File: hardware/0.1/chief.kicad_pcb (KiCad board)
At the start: 2 copper layers, 84.3 x 65 mm, 54 parts, among them J1 USB_C_Receptacle_USB2.0, Q1 DTC123J, Q2 BSS138, SW1 Encoder_MX_RGB, SW10 Encoder_MX_RGB, SW11 MX_RGB, SW12 MX_RGB, SW13 SW_Push, SW2 MX_RGB, SW3 MX_RGB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

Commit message: sorry Bing
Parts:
- removed RN5: 5K1, Resistor_SMD:R_Array_Convex_4x0603
- added R6: 5K1, Resistor_SMD:R_0603_1608Metric, B.Cu at (147.1, 74.8)
- added R7: 5K1, Resistor_SMD:R_0603_1608Metric, B.Cu at (145.6, 74.8)
- moved C13 32.2 mm to (174.1, 82.1), turned to 90 degrees
- moved C6 30.3 mm to (111.6, 82.1), turned to 90 degrees
- moved C5 29.9 mm to (160.6, 73.3), turned to 0 degrees
- moved C10 25.3 mm to (116.9, 82.1), turned to 90 degrees
- moved C9 24.7 mm to (168.8, 82.1), turned to 90 degrees
- moved C1 20.2 mm to (140.2, 77.0), turned to 0 degrees
- moved U1 17.5 mm to (140.4, 79.8), turned to 270 degrees
- moved C12 16.2 mm to (155.0, 82.1), turned to 90 degrees
- moved C14 15.0 mm to (135.1, 97.9), turned to 180 degrees
- moved C7 14.9 mm to (130.7, 82.1), turned to 90 degrees
- moved C2 14.7 mm to (140.3, 82.5), turned to 0 degrees
- moved C11 11.4 mm to (135.9, 82.1)
- moved C8 11.4 mm to (149.7, 82.1)
- moved C3 7.93 mm to (139.8, 68.5)
- moved R2 6.03 mm to (160.6, 71.7)
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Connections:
- J1 pad A8: Net-(J1-PadA8) -> (no net)
- J1 pad B8: Net-(J1-PadB8) -> (no net)
- SW12 pad 4: Net-(SW12-Pad4) -> (no net)
- U1 pad 4: Net-(U1-Pad4) -> (no net)
- U3 pad 10: /SW12 -> (no net)
- U3 pad 11: Net-(U3-Pad11) -> (no net)
- U3 pad 12: Net-(U3-Pad12) -> (no net)
- U3 pad 13: Net-(U3-Pad13) -> (no net)
- U3 pad 2: /SW9 -> (no net)
- U3 pad 21: Net-(U3-Pad21) -> (no net)
- U3 pad 22: Net-(U3-Pad22) -> (no net)
- U3 pad 26: /SW5 -> /ENC2B_DB
- U3 pad 27: /ENC2B_DB -> /SW5
- U3 pad 3: /SW11 -> (no net)
- U3 pad 30: Net-(U3-Pad30) -> (no net)
- U3 pad 31: Net-(U3-Pad31) -> (no net)
- U3 pad 4: Net-(U3-Pad4) -> (no net)
- U3 pad 41: Net-(U3-Pad41) -> /ENC4A_DB
- U3 pad 42: /ENC4A_DB -> /ENC4B_DB
- U3 pad 43: Net-(U3-Pad43) -> /SW11
- U3 pad 45: Net-(U3-Pad45) -> /SW12
- U3 pad 46: /ENC4B_DB -> /SW9
- U3 pad 5: Net-(U3-Pad5) -> (no net)
- U3 pad 6: Net-(U3-Pad6) -> (no net)
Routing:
- net +5V: track 324.2 -> 171.7 mm, vias 12 -> 11
- net /LED1: track 102.6 -> 0.00 mm, vias 2 -> 0
- net GND: track 147.0 -> 46.0 mm, vias 16 -> 42
- net /LED2: track 86.2 -> 0.00 mm
- net Net-(SW4-Pad2): track 48.8 -> 0.00 mm, vias 2 -> 0
- net Net-(SW10-Pad1): track 40.8 -> 0.00 mm, vias 2 -> 0
- net Net-(SW1-Pad2): track 39.9 -> 0.00 mm, vias 4 -> 0
- net Net-(SW11-Pad3): track 39.8 -> 0.00 mm, vias 2 -> 0
- net Net-(SW5-Pad4): track 35.2 -> 0.00 mm, vias 2 -> 0
- net /SW12: track 45.8 -> 28.3 mm
- net Net-(SW6-Pad4): track 45.9 -> 28.5 mm, vias 2 -> 0
- net /SW11: track 49.6 -> 36.4 mm
- net /BOOT0: track 35.3 -> 48.4 mm
- net Net-(SW2-Pad4): track 40.1 -> 29.0 mm, vias 3 -> 2
- net Net-(J1-PadB5): track 19.2 -> 8.62 mm
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
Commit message: moar layout
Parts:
- added D3: WS2812B, LED_SMD:LED_WS2812B_PLCC4_5.0x5.0mm_P3.2mm, B.Cu at (161.9, 104.5)
- added D4: WS2812B, LED_SMD:LED_WS2812B_PLCC4_5.0x5.0mm_P3.2mm, B.Cu at (124.8, 82.0)
- added D5: WS2812B, LED_SMD:LED_WS2812B_PLCC4_5.0x5.0mm_P3.2mm, B.Cu at (123.8, 104.5)
- added D6: WS2812B, LED_SMD:LED_WS2812B_PLCC4_5.0x5.0mm_P3.2mm, B.Cu at (160.1, 82.0)
- added H5: dan, graphics:danandrews, F.Cu at (142.6, 90.7)
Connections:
- SW12 pad 4: (no net) -> /BKLT
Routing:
- net +5V: track 171.7 -> 281.0 mm, vias 11 -> 20
- net /LED2: track 0.00 -> 88.0 mm, vias 0 -> 2
- net /LED1: track 0.00 -> 71.7 mm, vias 0 -> 4
- net Net-(SW5-Pad4): track 0.00 -> 48.5 mm, vias 0 -> 7
- net Net-(SW4-Pad2): track 0.00 -> 45.3 mm, vias 0 -> 2
- net Net-(SW1-Pad2): track 0.00 -> 44.5 mm, vias 0 -> 4
- net Net-(SW10-Pad1): track 0.00 -> 44.2 mm, vias 0 -> 4
- net Net-(SW11-Pad3): track 0.00 -> 29.0 mm, vias 0 -> 2
- net GND: track 46.0 -> 51.8 mm, vias 42 -> 46
- net /SW1: track 49.4 -> 50.9 mm
- net /LED: track 36.8 -> 35.5 mm
- net +3V3: track 183.2 -> 184.3 mm
- net /ENC3B_DB: track 24.7 -> 25.7 mm
- net /ENC3A_DB: track 20.6 -> 21.6 mm
- net /SW2: track 30.6 -> 30.0 mm
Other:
- board text added: "CHIEF"
- board text added: "LED"
- board text added: "PWR"
- board text added: "RST"
- board text added: "bing"

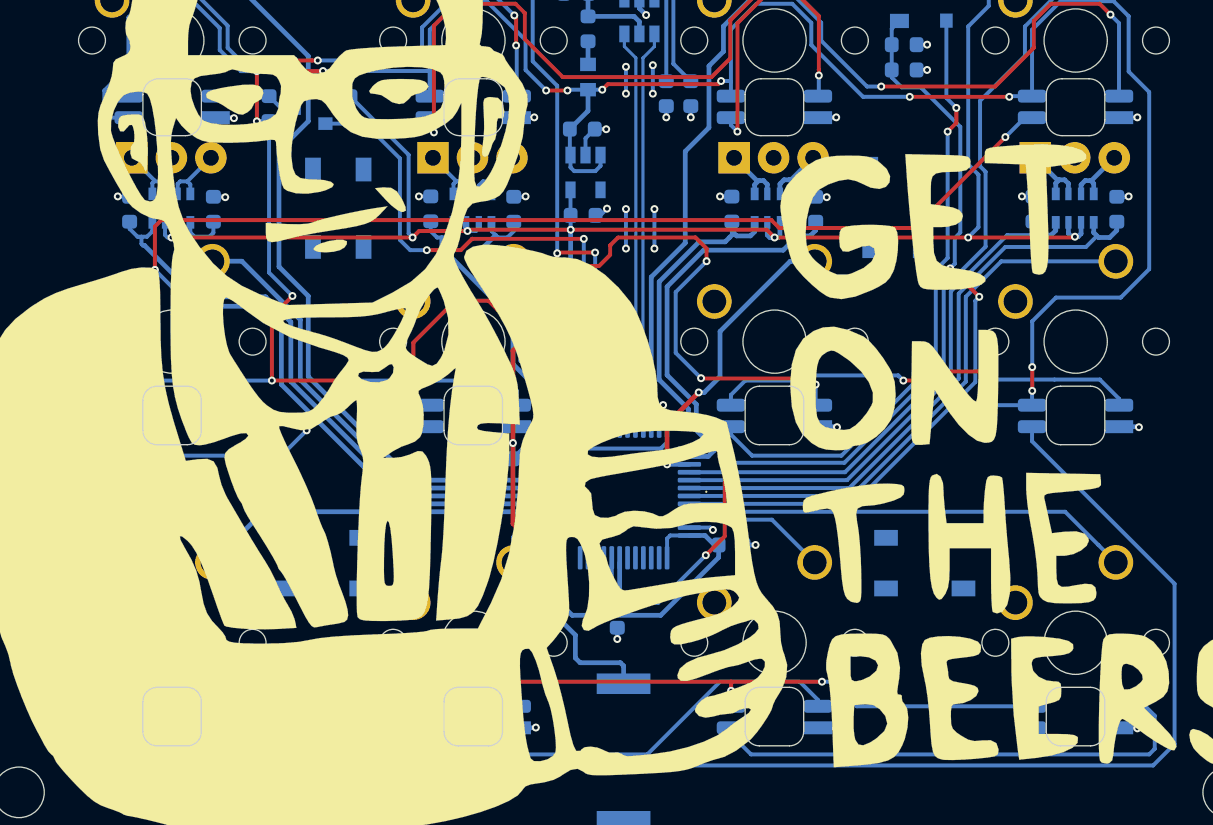
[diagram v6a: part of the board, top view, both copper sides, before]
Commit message: LEDs connected, adjustments to LED/text/image position
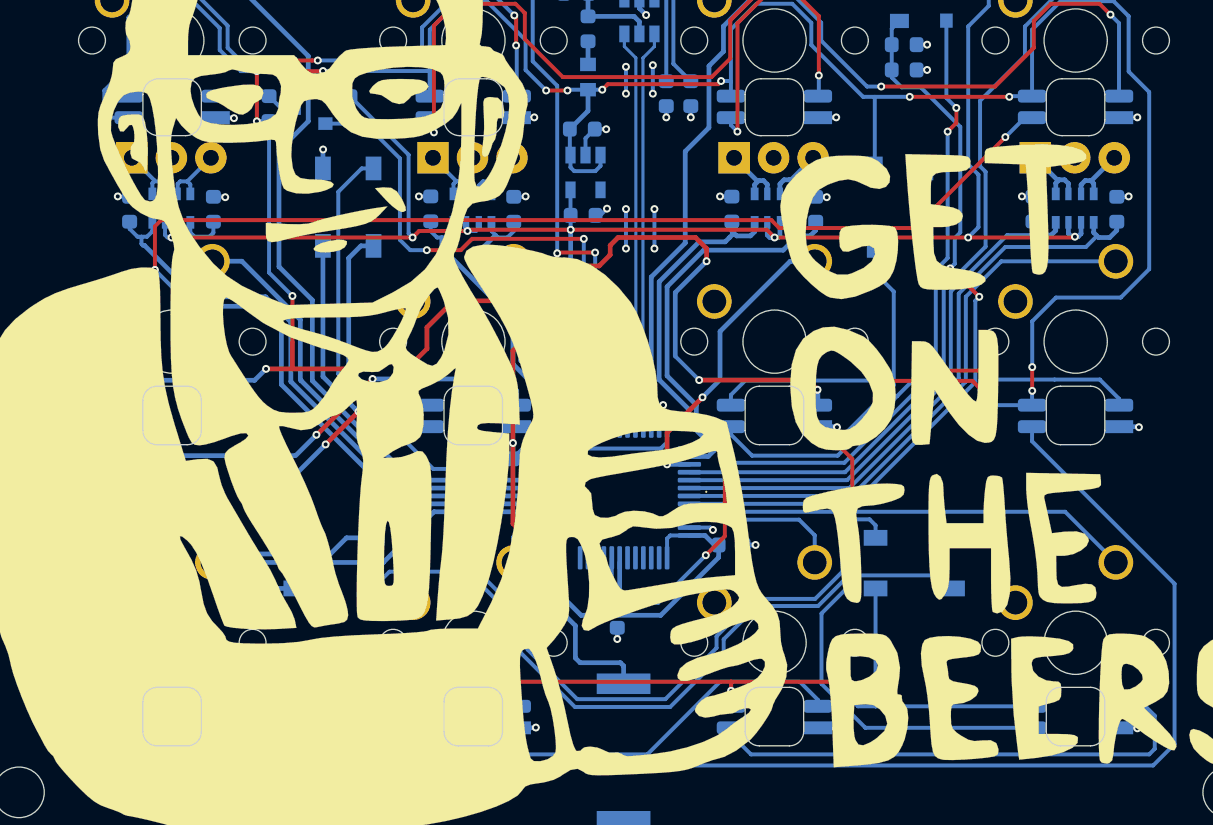
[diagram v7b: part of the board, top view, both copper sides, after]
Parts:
- moved D5 0.73 mm to (124.5, 104.5)
- moved D3 0.66 mm to (161.2, 104.5)
- moved D4 0.63 mm to (125.4, 82.0)
- moved D6 0.29 mm to (160.3, 82.0)
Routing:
- net Net-(D3-Pad2): track 0.00 -> 68.8 mm, vias 0 -> 2
- net Net-(D5-Pad2): track 0.00 -> 62.5 mm, vias 0 -> 2
- net +5V: track 281.0 -> 316.4 mm
- net /BKLT: track 0.00 -> 28.6 mm
- net Net-(D4-Pad2): track 0.00 -> 21.1 mm, vias 0 -> 2
- net GND: track 51.8 -> 56.8 mm, vias 46 -> 50
- net /SW9: track 9.05 -> 10.1 mm
- net Net-(SW5-Pad4): track 48.5 -> 48.6 mm, vias 7 -> 6
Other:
- board text added: "opsbinxu"

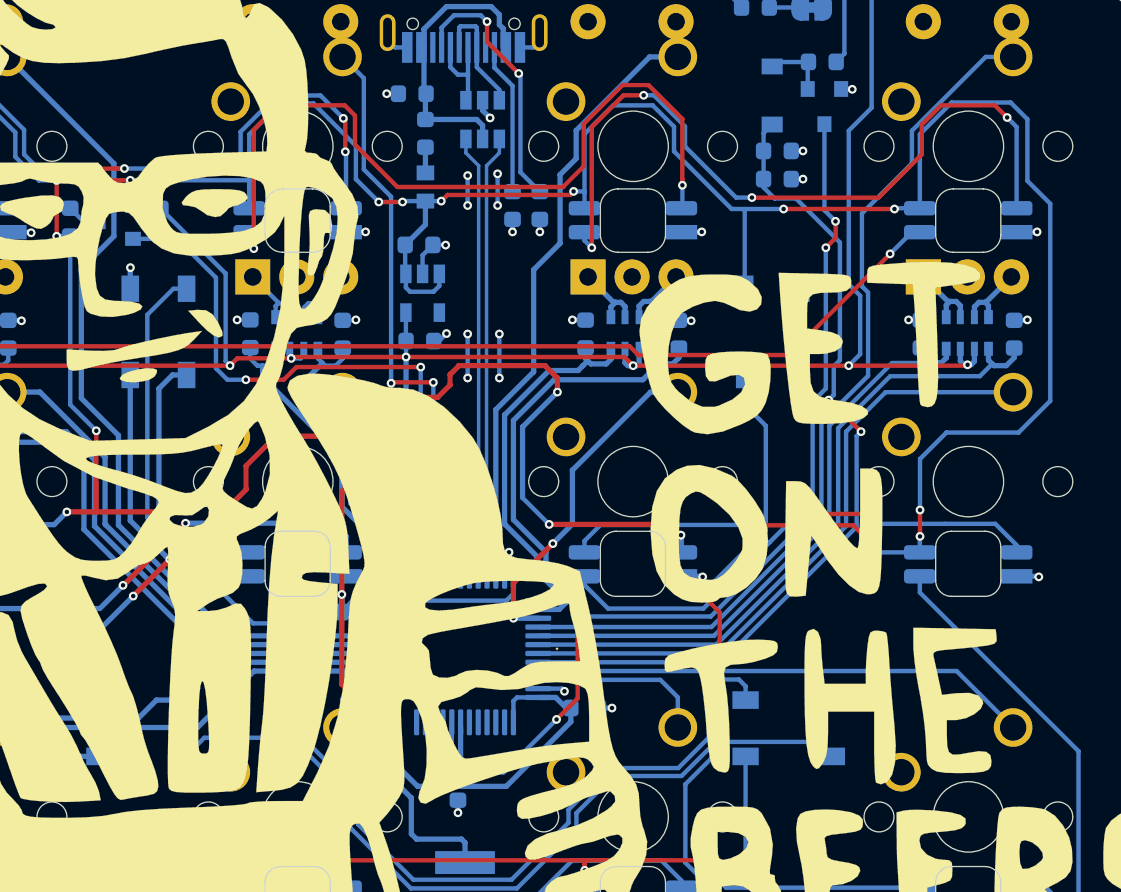
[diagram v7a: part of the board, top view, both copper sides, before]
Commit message: LED positioning
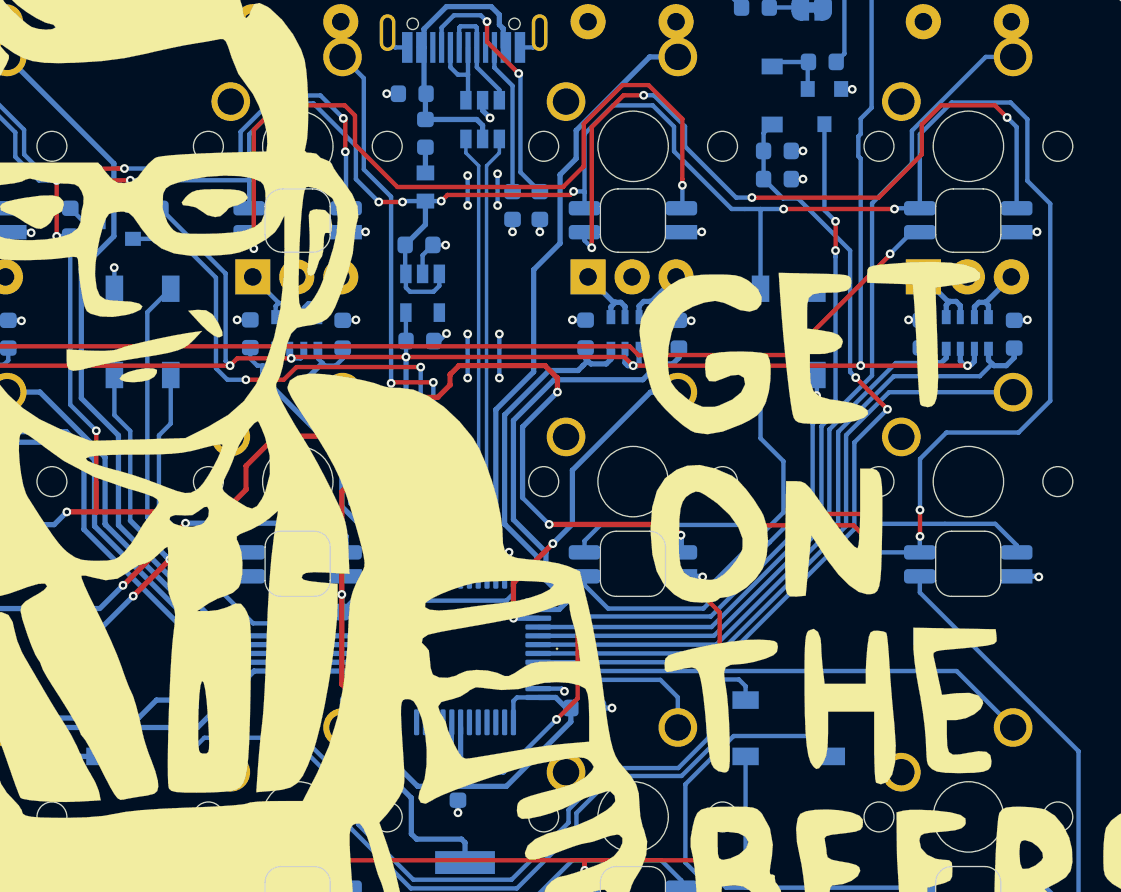
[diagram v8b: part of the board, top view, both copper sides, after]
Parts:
- moved D4 0.90 mm to (124.5, 82.0)
- moved D6 0.90 mm to (161.2, 82.0)
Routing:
- net +5V: track 316.4 -> 315.6 mm
- net Net-(D3-Pad2): track 68.8 -> 67.9 mm
- net +3V3: track 184.0 -> 183.2 mm
